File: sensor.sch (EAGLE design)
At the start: 18 parts

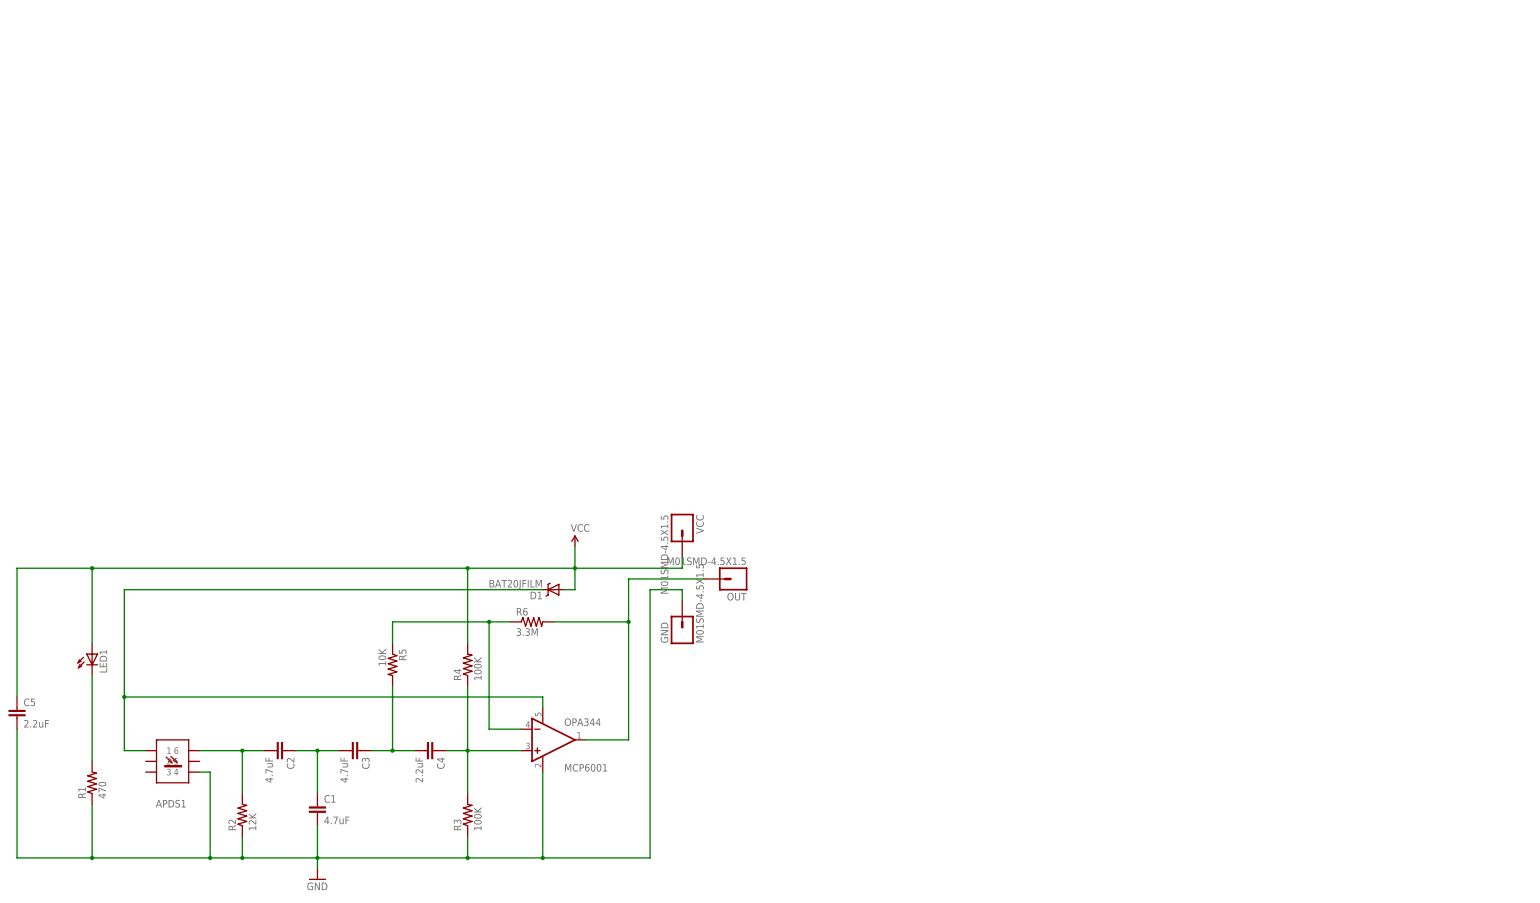
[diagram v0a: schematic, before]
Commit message: pulled down all the eagle files on github.  histogram.py generates a histogram of the frequency of their usage.  You can make all the boards on github with ~1460 unique parts
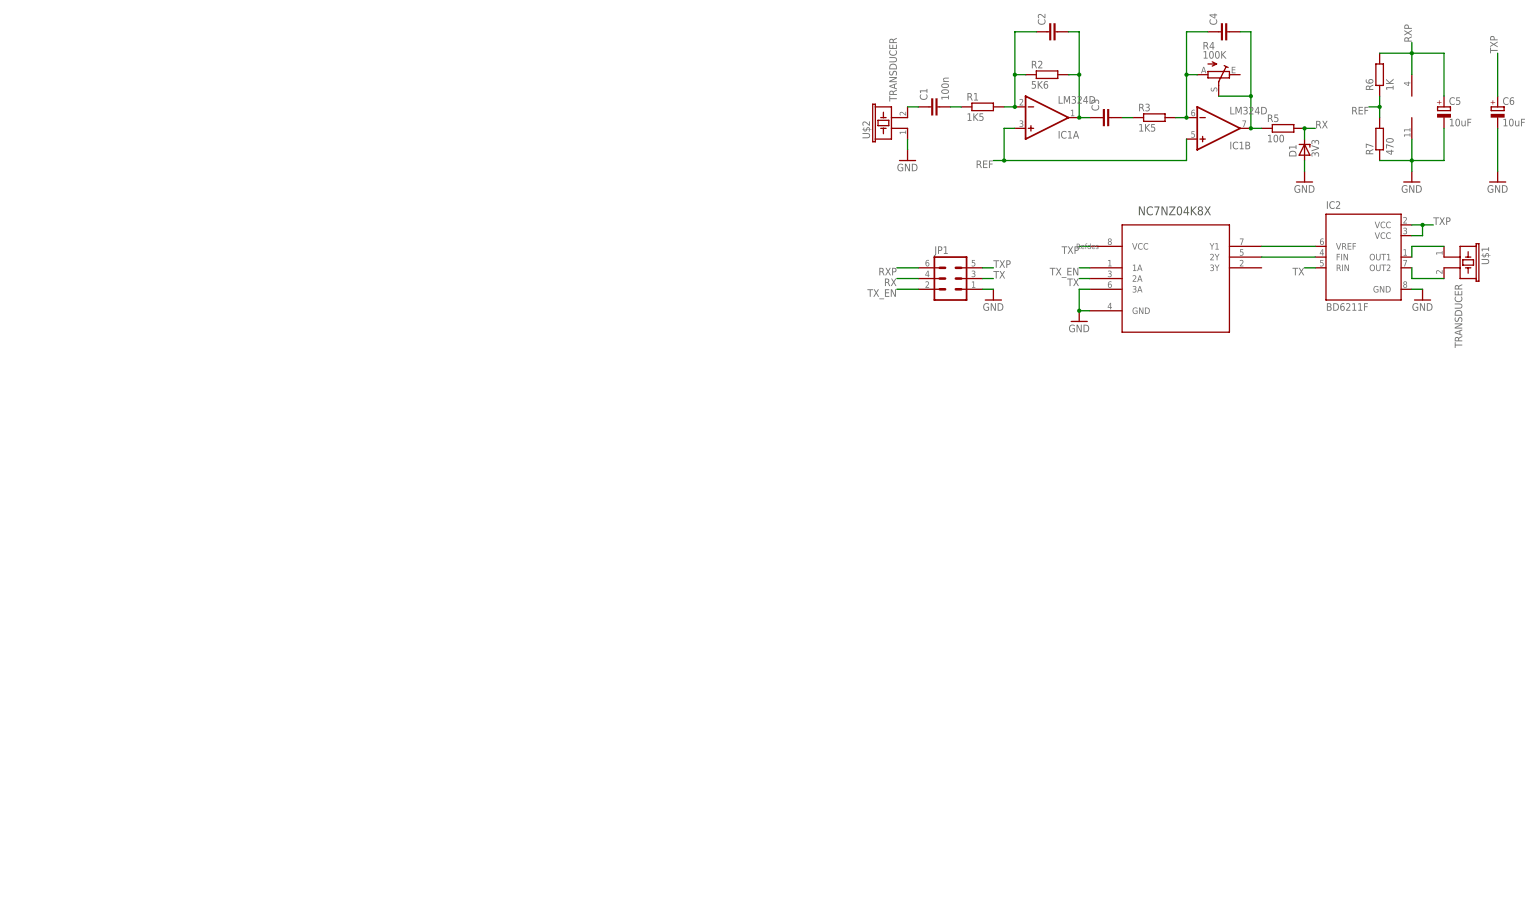
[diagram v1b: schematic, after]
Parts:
- removed APDS1: (no value), librae:APDS-9008
- removed GND, OUT, VCC: M01SMD-4.5X1.5, SparkFun-Connectors:M01SMD-4.5X1.5
- removed LED1: (no value), librae:LED
- removed MCP6001: OPA344, SparkFun-AnalogIC:OPA344
- added C6: 10uF, rcl:CPOL-EUE2-5
- added IC1: LM324D, linear:LM324D
- added IC2: BD6211F, Ultrasound:BD6211F
- added JP1: (no value), con-lstb:MA03-2
- added R7: 470, rcl:R-EU_R0805
- added U$1, U$2: TRANSDUCER, Ultrasound:TRANSDUCER
- added U1: NC7NZ04K8X, Ultrasound:NC7NZ04K8X
- C1: value 4.7uF -> 100n; device SparkFun-Capacitors:1.0UF-16V-10%(0603) -> rcl:C-EUC0805
- C2, C3: value 4.7uF -> (none); device SparkFun-Capacitors:1.0UF-16V-10%(0603) -> rcl:C-EUC0805
- C4: value 2.2uF -> (none); device SparkFun-Capacitors:1.0UF-16V-10%(0603) -> rcl:C-EUC0805; PROD_ID CAP-00868 -> (none); VALUE 1.0uF -> (none)
- C5: value 2.2uF -> 10uF; device SparkFun-Capacitors:1.0UF-16V-10%(0603) -> rcl:CPOL-EUE2-5; PROD_ID CAP-00868 -> (none); VALUE 1.0uF -> (none)
- D1: value BAT20JFILM -> 3V3; device SparkFun-DiscreteSemi:BAT20JFILM -> diode:ZENER-DIODEZD-2.5
- R1: value 470 -> 1K5; device SparkFun-Resistors:10KOHM1/10W1%(0603)0603 -> rcl:R-EU_R0805
- R2: value 12K -> 5K6; device SparkFun-Resistors:10KOHM1/10W1%(0603)0603 -> rcl:R-EU_R0805
- R3: value 100K -> 1K5; device SparkFun-Resistors:10KOHM1/10W1%(0603)0603 -> rcl:R-EU_R0805
- R4: device SparkFun-Resistors:10KOHM1/10W1%(0603)0603 -> pot:TRIM_EU-S63P
- R5: value 10K -> 100; device SparkFun-Resistors:10KOHM1/10W1%(0603)0603 -> rcl:R-EU_R0805
- R6: value 3.3M -> 1K; device SparkFun-Resistors:10KOHM1/10W1%(0603)0603 -> rcl:R-EU_R0805; PROD_ID RES-00824 -> (none); VALUE 10K -> (none)
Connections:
- removed net N$8: C1.1, C2.1, C3.2
- removed net OUT: MCP6001.OUT, OUT.1, R6.2
- removed net VCC: C5.1, D1.A, LED1.A, R4.2, VCC.1
- removed net VDD: APDS1.1, D1.C, MCP6001.V+
- new net N$1: C2.1, IC1A.-IN, R1.2, R2.1
- new net N$11: IC2.OUT2, U$1.2
- new net N$12: IC2.VREF, U1.Y1
- new net N$13: IC2.FIN, U1.2Y
- new net N$2: C1.2, R1.1
- new net N$5: C3.2, R3.1
- new net REF: IC1A.+IN, IC1B.+IN, R6.1, R7.2
- new net RX: D1.C, JP1.4, R5.2
- new net RXP: C5.+, IC1P.V+, JP1.6, R6.2
- new net TX: IC2.RIN, JP1.3, U1.2A
- new net TXP: C6.+, IC2.VCC@1, IC2.VCC@2, JP1.5, U1.VCC
- new net TX_EN: JP1.2, U1.1A
- net GND: now also C5.-, C6.-, D1.A, IC1P.V-, IC2.GND, JP1.1, R7.1, U$2.1, U1.3A, U1.GND; no longer APDS1.4, C1.2, C5.2, GND.1, MCP6001.V-, R1.1, R2.1, R3.1
- net N$10: now also IC2.OUT1, U$1.1; no longer C4.1, MCP6001.+IN, R3.2, R4.1
- net N$3: now also C2.2, C3.1, IC1A.OUT, R2.2; no longer LED1.C, R1.2
- net N$6: now also C4.1, IC1B.-IN, R3.2, R4.A; no longer MCP6001.-IN, R5.1, R6.1
- net N$7: now also C4.2, IC1B.OUT, R4.S, R5.1; no longer APDS1.6, C2.2, R2.2
- net N$9: now also C1.1, U$2.2; no longer C3.1, C4.2, R5.2
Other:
- moved on the sheet: C1, C2, C3, C4
